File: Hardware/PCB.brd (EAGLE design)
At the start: 46 x 35 mm, 61 parts, among them IC1 BQ25180, IC3 BMA421, IC4 DRV2605, IC9 RT6160, J1 TC2030, J3 FPC-24P, J5 USB-C, Q2 SI1308EDL, Q4 MOSFET-N, U1 NRF52840_QF, U2 MAX17048G+T10, X2 32MHz

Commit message: fixing issues #25 and partially #15 in pcb
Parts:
- added C1-EP-DR1: 10uF, Tinkercad:CAPC1005X60
- added C19: 100nF, Tinkercad:CAPC1005X60
- added C2-EP-DR1: 4.7uF/25V, Tinkercad:CAPC1005X60
- added C20, C21: 4.7μF, Tinkercad:CAPC1005X60
- added EPD_C13: 0.1uF/50V, Tinkercad:CAPC1005X60
- added EPD_C14, EPD_C15, EPD_C16, EPD_C17, EPD_C18, EPD_C19, EPD_C20, EPD_C3, EPD_C4: 1uF/50V, Tinkercad:CAPC1005X60
- added R1, R10, R6: 10k, InkTime_v5:CPF0201D7K68C1_0201
- added R17, R18: 3K3, InkTime_v5:CPF0201D7K68C1_0201
- added R1_EP_DR1: 0.47, InkTime_v5:CPF0201D7K68C1_0201
- added R1_USB1, R2_USB1: 5K1, InkTime_v5:CPF0201D7K68C1_0201
- added R2, R3, R4: 0, InkTime_v5:CPF0201D7K68C1_0201
- added R2_EP_DR1, R9: 10K, InkTime_v5:CPF0201D7K68C1_0201
- added SJ1: 0, InkTime_v5:ESP32_C6_LIBRARY_7_JUMPER_SJ
- added TP1, TP2, TP3, TP4, TP5, TP6, TP7, TP8, TP_BAT_GND1, TP_ON1, TP_OP1, TP_SCL, TP_SDA, TP_VBAT1: HECTOR_WATCH_1_TPTP20R, InkTime_v5:HECTOR_WATCH_1_TP20R
- added U$1: (no value), InkTime_v5_button fara modifcaturi:NORDIC_NRF_BT-XTAL_2016_N
- ANT1: value ANT -> 2450AT18B100E
- C10, C13, C22: value NC -> N.C.
- C14, C6: value 4.7uF -> 4.7μF
- C15: value 1uF -> 1.0μF
- C9: value 820pF -> 820pF N.C.
- D8: value USBLC6-2 -> USBLC6-2SC6Y
- IC1: value BQ25180 -> BQ25180YBGR
- IC4: value DRV2605 -> DRV2605YZFR
- IC9: value RT6160 -> RT6160AWSC
- J1: value TC2030 -> TC2030-IDC_TC2030-IDC
- J3: value FPC-24P -> 503480-2400
- J5: value USB-C -> KH-TYPE-C-16P
- L2: value 10uH -> 10μH
- L7: value 0.47uH -> FTC252012SR47MBCA
- Q2: value SI1308EDL -> SI1308EDL-T1-GE3
- Q4: value MOSFET-N -> 20V/4.2A/52mΩ/1.4W
- SW_DN, SW_ENT, SW_UP: value EVP-AKE31A -> 2025-10-22_07-23-44_LIBRARY_EVP-AKE31ASW_EVP-AKE31A_PAN
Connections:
- net SIG_VREG_FEED renamed N$1
- new net 3V3/1.7D2: C40.2, IC4.A2
- new net ALERT: U1.P$J24, U2.5
- new net D+: D8.4, U1.P$AD6
- new net D-: D8.6, U1.P$AD4
- new net DEC1: C5.2, U1.P$C1
- new net DEC3: C11.1, U1.P$D23
- new net DEC4_6: C10.1, C15.2, C16.1, L3.2, U1.P$B5, U1.P$E24
- new net DN: D8.1, J5.A7, J5.B7
- new net DP: D8.3, J5.A6, J5.B6
- new net EPD_3V3: C1-EP-DR1.2, EPD_C13.2, J3.15, J3.16, L4.P$1, Q4.3
- new net EPD_BUSY: J3.9, U1.P$AD12
- new net EPD_CS: J3.12, U1.P$K2
- new net EPD_DC: J3.11, U1.P$AD10
- new net EPD_RST: J3.10, U1.P$AC11
- new net GDR: J3.2, Q2.1, R2_EP_DR1.2
- new net HAPTIC_EN: IC4.A1, U1.P$U1
- new net IMU_INT1: IC3.5, U1.P$N1
- new net IMU_INT2: IC3.6, U1.P$P2
- new net LX1: IC9.B2, IC9.B3, L7.1
- new net LX2: IC9.D2, IC9.D3, L7.2
- new net MOSI: J3.14, U1.P$B13
- new net N$10: C9.1, U1.P$N24
- new net N$2: IC9.E1, R2.2
- new net N$22: C2-EP-DR1.1, D7.2, L4.P$2, Q2.3
- new net N$23: R1_EP_DR1.1, R_TYPE_SEL1.2, SJ1.2
- new net N$24: C2-EP-DR1.2, D1.1, D6.2
- new net N$25: EPD_C3.2, J3.4
- new net N$26: EPD_C4.2, J3.5
- new net N$27: EPD_C14.2, J3.18
- new net N$28: EPD_C15.2, J3.19
- new net N$29: EPD_C16.2, J3.20
- new net N$3: IC3.1, R3.2
- new net N$30: EPD_C18.2, J3.22
- new net N$31: EPD_C20.2, J3.24
- new net N$32: J5.A5, R1_USB1.2
- new net N$33: J5.B5, R2_USB1.1
- new net N$34: IC4.C3
- new net N$38: C20.1, U1.P$AC5
- new net N$4: C3.1, L1.1, U1.P$H23
- new net N$5: ANT1.1, C22.1, C4.1, L1.2
- new net N$56: L2.2, L3.1
- new net N$57: L2.1, U1.P$B3
- new net N$7: IC1.D1, R9.2
- new net N$71: C13.1, U1.P$A18
- new net N$74: C2.2, U$1.3, U1.P$A23
- new net N$75: C1.2, U$1.1, U1.P$B24
- new net OUT+: IC4.A3, TP_OP1.TP
- new net OUT-: TP_ON1.TP
- new net P0.00/XL1: C17.2, U1.P$D2, X2.3
- new net P0.01/XL2: C18.1, U1.P$F2, X2.1
- new net P0.04: U1.P$J1
- new net P0.09: U1.P$L24
- new net P0.13: C41.2, R1.1, SW_UP.2, U1.P$AD8
- new net P0.14: C44.2, R6.1, SW_ENT.2, U1.P$AC9
- new net P0.19: U1.P$AC15
- new net P0.20: U1.P$AD16
- new net P0.21: U1.P$AC17
- new net P0.22: U1.P$AD18
- new net P0.23: U1.P$AC19
- new net P0.24: U1.P$AD20
- new net P0.25: U1.P$AC21
- new net P0.26: U1.P$G1
- new net P0.27: U1.P$H2
- new net P0.28: U1.P$B11
- new net P0.29: U1.P$A10
- new net P0.30: U1.P$B9
- new net P0.31: U1.P$A8
- new net P1.01: Q4.1, R_PWR_EPD1.1, U1.P$Y23
- new net P1.02: C45.2, R10.1, SW_DN.2, U1.P$W24
- new net P1.03: U1.P$V23
- new net P1.04: U1.P$U24
- new net P1.05: U1.P$T23
- new net P1.06: U1.P$R24
- new net P1.07: U1.P$P23
- new net P1.09: U1.P$R1
- new net P1.10: U1.P$A20
- new net P1.11: U1.P$B19
- new net P1.12: U1.P$B17
- new net P1.13: U1.P$A16
- new net P1.14: U1.P$B15
- new net P1.15: U1.P$A14
- new net PMIC_INIT: IC1.A1
- new net PMIC_INT: U1.P$T2
- new net PREVGH: D7.1, EPD_C17.2, J3.21
- new net PREVGL: D1.2, EPD_C19.2, J3.23
- new net RESE: J3.3, Q2.2, R1_EP_DR1.2
- new net RESET: J1.6, TP5.TP, U1.P$AC13
- new net SCK: J3.13, U1.P$A12
- new net SCL: IC1.B1, IC3.12, IC4.C1, R17.2, R4.1, TP_SCL.TP, U1.P$M2, U2.7
- new net SDA: IC1.C1, IC3.2, IC4.B2, R18.2, R2.1, TP_SDA.TP, U1.P$L1, U2.8
- new net SWDCLK: J1.4, TP6.TP, U1.P$AA24
- new net SWDIO: J1.2, TP3.TP, U1.P$AC24
- new net SWO: TP4.TP, U1.P$AD22
- new net VBAT: C26.2, C37.2, IC1.C2, TP_VBAT1.TP, U2.2, U2.3
- new net VREG: C23.1, C24.2, C39.1, IC1.B2, IC9.A1, IC9.A2, IC9.A3, TP2.TP
- net 3V3: now also C12.1, C14.2, C19.2, C25.2, C33.1, C36.2, C6.1, C7.1, C8.1, IC3.10, IC3.3, IC3.7, IC4.C2, IC9.E3, J1.1, Q4.2, R1.2, R10.2, R17.1, R18.1, R6.2, R_PWR_EPD1.2, TP1.TP, TP7.TP, U1.P$AD14, U1.P$AD23, U1.P$B1, U1.P$W1, U1.P$Y2
- net GND: now also C1-EP-DR1.1, C1.1, C10.2, C11.2, C12.2, C13.2, C14.1, C15.1, C16.2, C17.1, C18.2, C19.1, C2.1, C20.2, C21.2, C22.2, C23.2, C24.1, C25.1, C26.1, C28.2, C3.2, C33.2, C35.2, C36.1, C37.1, C38.1, C4.2, C40.1, C41.1, C44.1, C45.1, C5.1, C6.2, C7.2, C8.2, C9.2, D6.1, D8.2, EPD_C13.1, EPD_C14.1, EPD_C15.1, EPD_C16.1, EPD_C17.1, EPD_C18.1, EPD_C19.1, EPD_C20.1, EPD_C3.1, EPD_C4.1, IC3.8, IC3.9, IC4.B1, IC4.B3, IC9.B1, IC9.C1, IC9.C2, IC9.C3, J1.3, J1.5, J3.17, J3.8, J3.MP1, J3.MP2, J5.A12_B1, J5.A1_B12, J5.SH1, J5.SH2, J5.SH3, J5.SH4, R1_USB1.1, R2_EP_DR1.1, R2_USB1.2, R3.1, R9.1, R_TYPE_SEL1.1, SJ1.1, SW_DN.1, SW_ENT.1, SW_UP.1, TP8.TP, TP_BAT_GND1.TP, U$1.2, U$1.4, U1.P$75, U1.P$76, U1.P$77, U1.P$78, U1.P$79, U1.P$80, U1.P$81, U1.P$82, U1.P$83, U1.P$84, U1.P$85, U1.P$86, U1.P$87, U1.P$88, U1.P$89, U1.P$90, U1.P$B7, U1.P$F23, U2.1, U2.4, U2.6, U2.9
- net VBUS: now also C21.1, C28.1, C35.1, C38.2, D8.5, J5.A9_B4, U1.P$AD2
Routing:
- net GND: track 0.00 -> 311.0 mm, vias 0 -> 20
- net 3V3: track 1.65 -> 151.8 mm, vias 0 -> 20
- net SDA: track 0.00 -> 90.8 mm, vias 0 -> 5
- net DEC4_6: track 0.00 -> 59.5 mm, vias 0 -> 2
- net VBUS: track 0.98 -> 59.3 mm, vias 0 -> 7
- net SCL: track 0.00 -> 56.2 mm, vias 0 -> 6
- net SWDCLK: track 0.00 -> 40.8 mm, vias 0 -> 4
- net P0.13: track 0.00 -> 40.7 mm, vias 0 -> 5
- net SWDIO: track 0.00 -> 36.8 mm, vias 0 -> 4
- net N$5: track 0.00 -> 34.9 mm, vias 0 -> 4
- net VREG: track 0.00 -> 32.6 mm, vias 0 -> 4
- net PREVGL: track 0.00 -> 29.9 mm, vias 0 -> 4
- net RESE: track 0.00 -> 28.2 mm
- net DP: track 0.00 -> 27.8 mm, vias 0 -> 2
- net EPD_3V3: track 0.00 -> 27.0 mm, vias 0 -> 2
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- added copper zone on layer 16, net GND
- added copper zone on layer 2, net GND

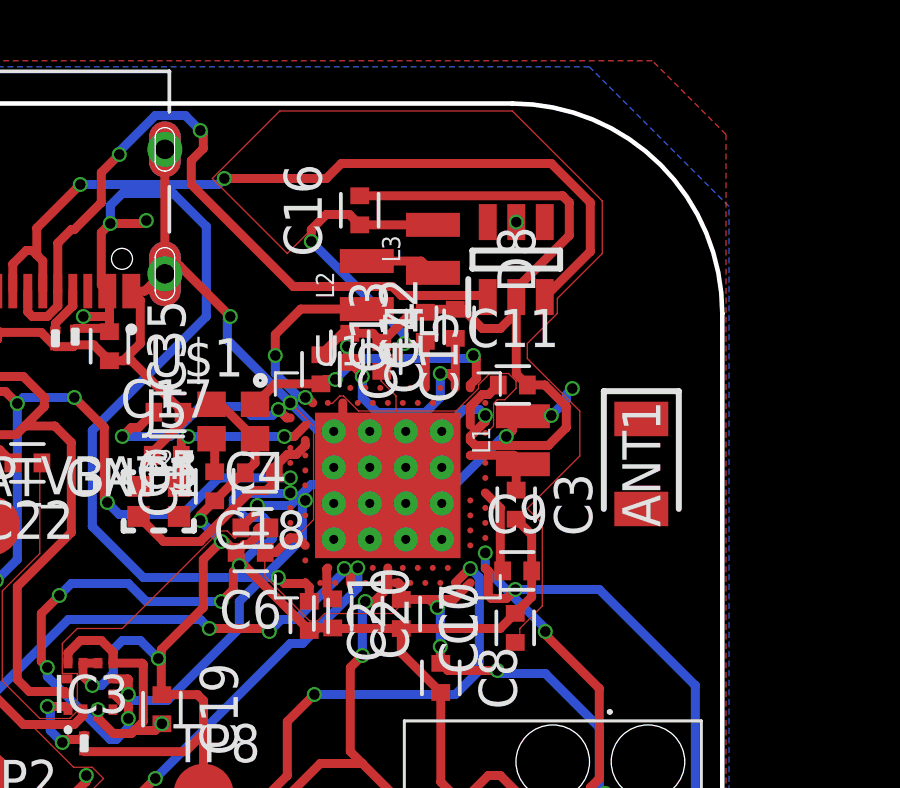
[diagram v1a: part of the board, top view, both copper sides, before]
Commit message: fixing issue #18 in pcb
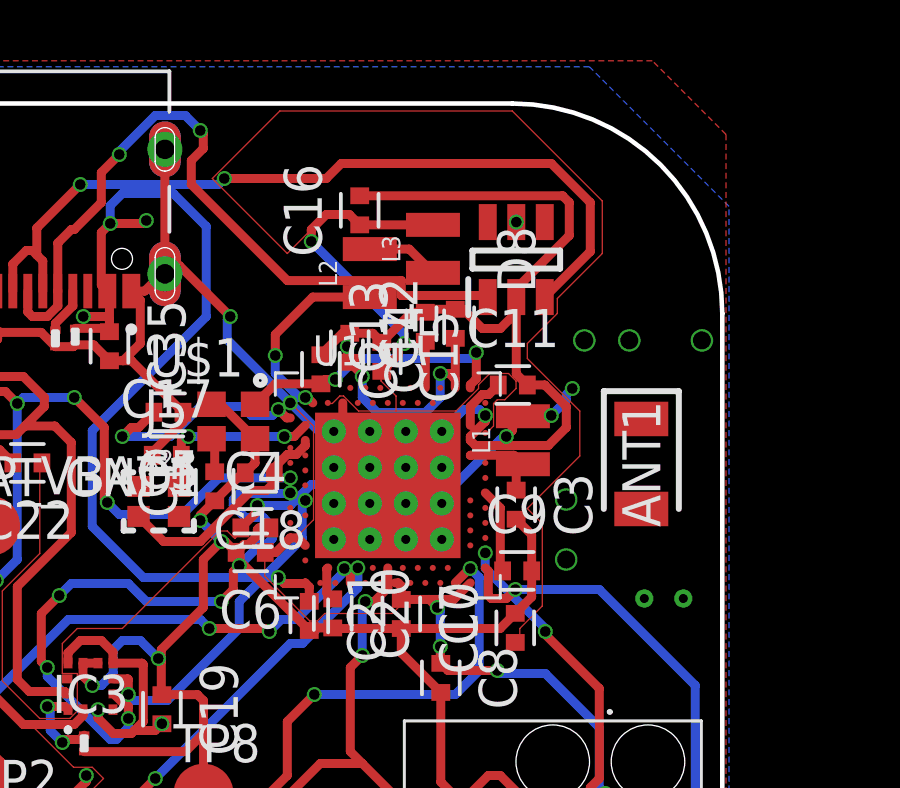
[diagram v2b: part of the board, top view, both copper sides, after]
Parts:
- moved L2 0.41 mm to (11.2, 11.8)
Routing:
- net GND: vias 20 -> 27

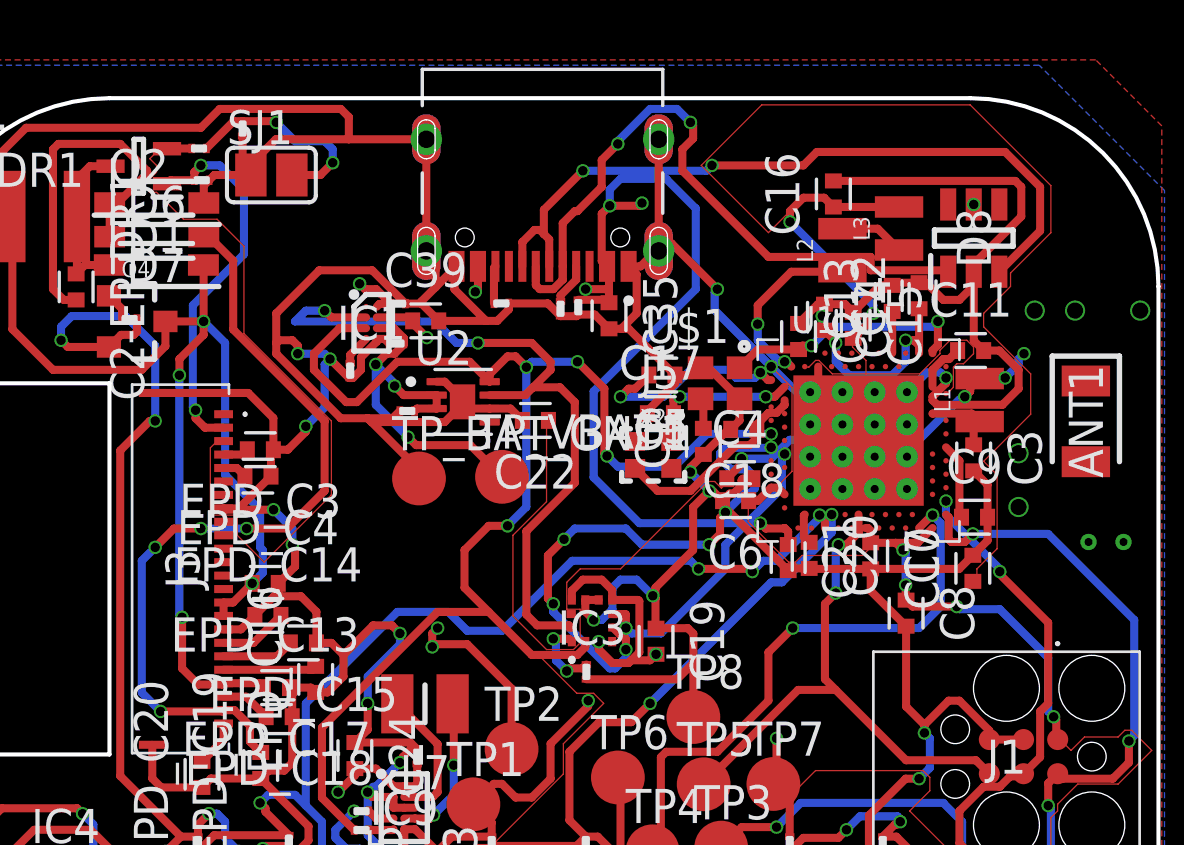
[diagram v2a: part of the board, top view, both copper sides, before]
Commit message: improve the bugs from issues #26 #16 #17 in pcb
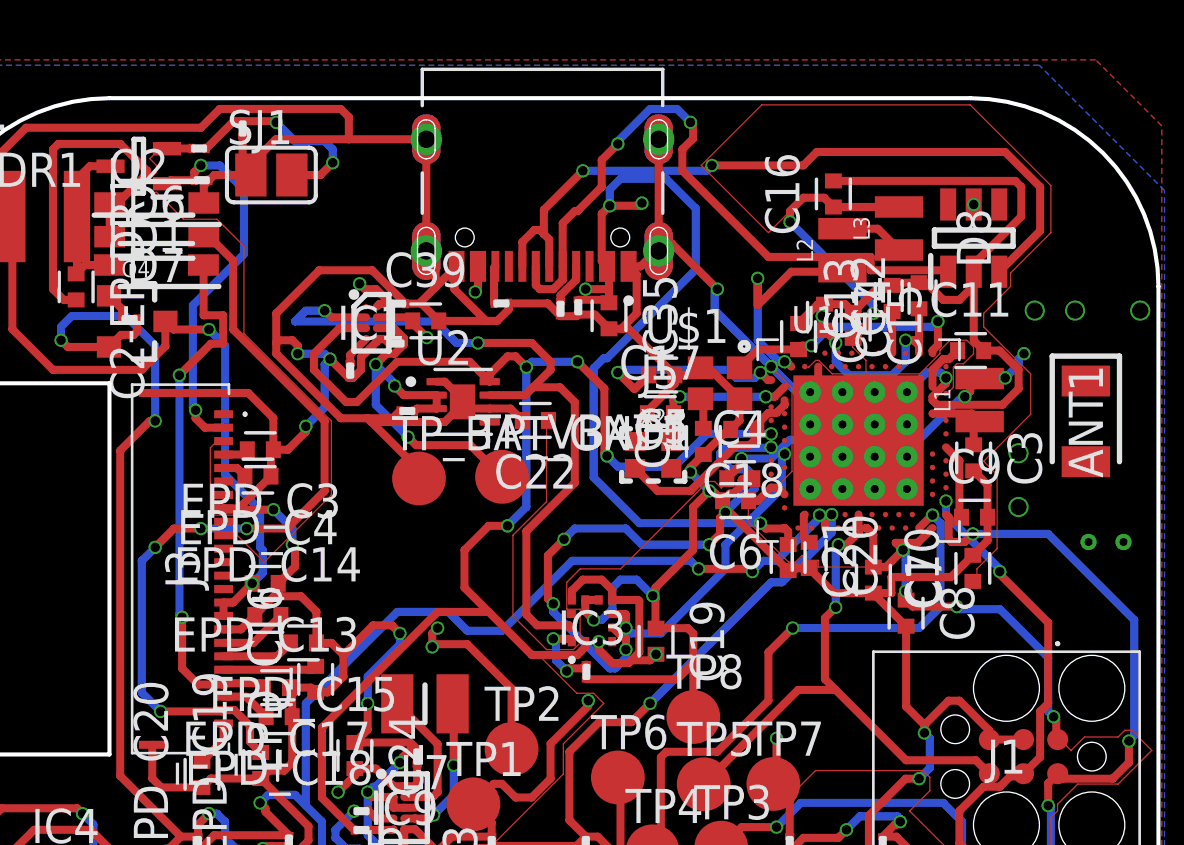
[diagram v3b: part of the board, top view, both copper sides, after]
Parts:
- moved C7 0.91 mm to (12.4, -0.42)
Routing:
- net N$57: track 6.62 -> 8.62 mm
- net 3V3: track 151.8 -> 153.3 mm
- net PREVGH: track 18.8 -> 20.1 mm
